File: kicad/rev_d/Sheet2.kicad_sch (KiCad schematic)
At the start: 186 parts, among them J10 vg_old, J5 external clock, J6 JUMPER, J8 JUMPER, J9 JUMPER, Q2 QUARTZ, Q3 QUARTZ32768, U2 PCA9555DB, X11 KEYB-MOUSE, X12 IDC20, X13 USB_C, X15 PLB2-2, X19 AVR pgm conn, X21 Turbosound conn, X22 PS2 extra input, X23 SEGA pads, X3 IDC26LPT, X4 IDC10M, X5 IDC10M, X6 RS232_9

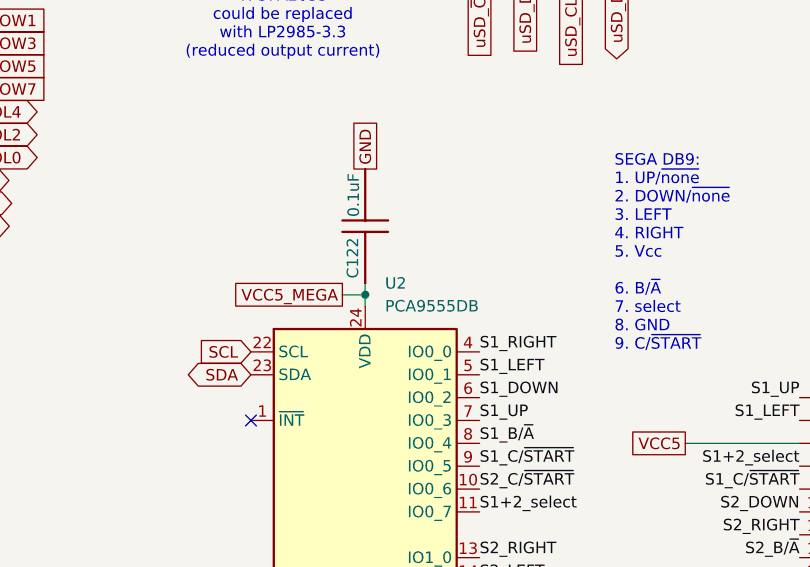
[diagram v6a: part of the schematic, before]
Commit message: pentevo: rev D: video output: make new sheet for video outputs
git-svn-id: svn://localhost/local-pentevo@1274 c6c76956-fad2-4150-a3a9-ea0a427205ba
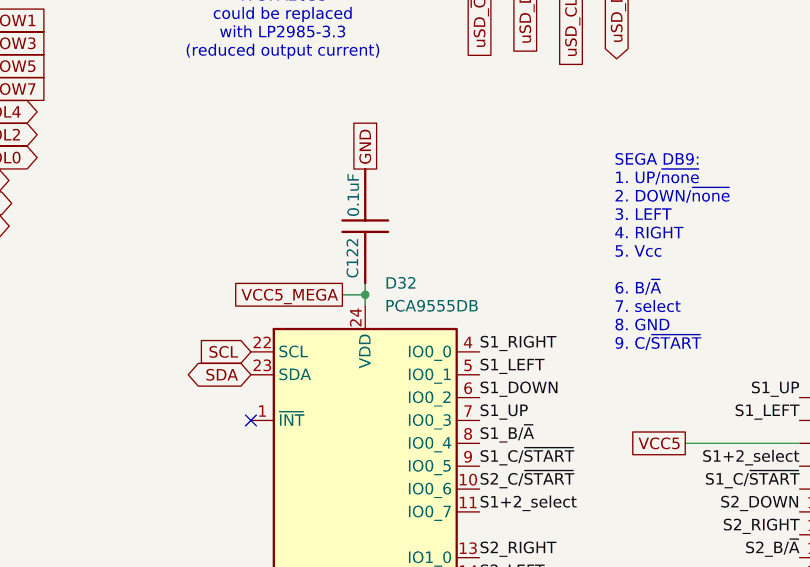
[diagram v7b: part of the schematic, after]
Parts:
- renumbered U2 to D32
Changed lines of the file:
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@@
 		(dnp no)
 		(fields_autoplaced yes)
-		(property "Reference" "U2"
+		(property "Reference" "D32"
 			(at 459.3941 146.05 0)
 			(effects
@@
 			(project ""
 				(path "/ab605654-a730-497b-9e09-9b351f74b935/31d5864f-06ec-4c73-9256-780a6880087d"
-					(reference "U2")
+					(reference "D32")
 					(unit 1)
 				)

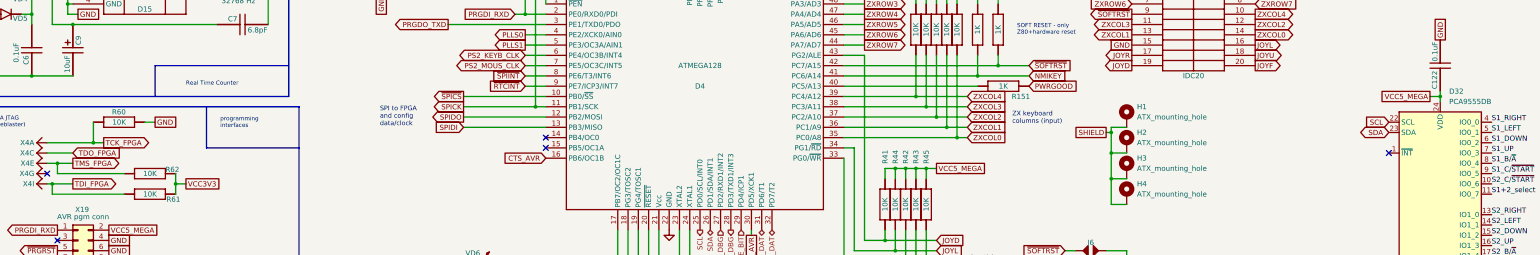
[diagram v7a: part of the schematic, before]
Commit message: pentevo: rev D: video output: remove 373/374 stuff (WIP); fix DA numbering issue
git-svn-id: svn://localhost/local-pentevo@1282 c6c76956-fad2-4150-a3a9-ea0a427205ba
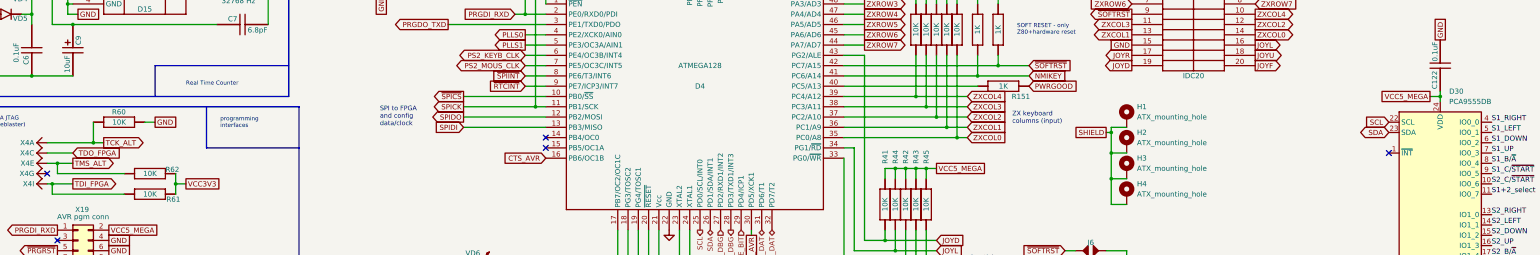
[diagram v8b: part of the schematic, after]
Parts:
- renumbered D32 to D30
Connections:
- net TCK_FPGA renamed TCK_ALT
- net TMS_FPGA renamed TMS_ALT
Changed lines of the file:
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@@
 		)
 	)
-	(global_label "TMS_FPGA"
+	(global_label "TMS_ALT"
 		(shape output)
 		(at 119.38 163.83 0)
@@
 		)
 		(property "Intersheetrefs" "${INTERSHEET_REFS}"
-			(at 131.6785 163.83 0)
+			(at 130.0456 163.83 0)
 			(effects
 				(font
@@
 		)
 	)
-	(global_label "TCK_FPGA"
+	(global_label "TCK_ALT"
 		(shape output)
 		(at 127 158.75 0)
@@
 		)
 		(property "Intersheetrefs" "${INTERSHEET_REFS}"
-			(at 139.1776 158.75 0)
+			(at 137.5447 158.75 0)
 			(effects
 				(font
@@
 		(dnp no)
 		(fields_autoplaced yes)
-		(property "Reference" "D32"
+		(property "Reference" "D30"
 			(at 459.3941 146.05 0)
 			(effects
@@
 			(project ""
 				(path "/ab605654-a730-497b-9e09-9b351f74b935/31d5864f-06ec-4c73-9256-780a6880087d"
-					(reference "D32")
+					(reference "D30")
 					(unit 1)
 				)
